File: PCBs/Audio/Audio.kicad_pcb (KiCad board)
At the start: 4 copper layers, 24.5 x 33.4 mm, 23 parts, among them J1 Conn_01x15, J2 Conn_01x02, U1 PTAS2780RYAR

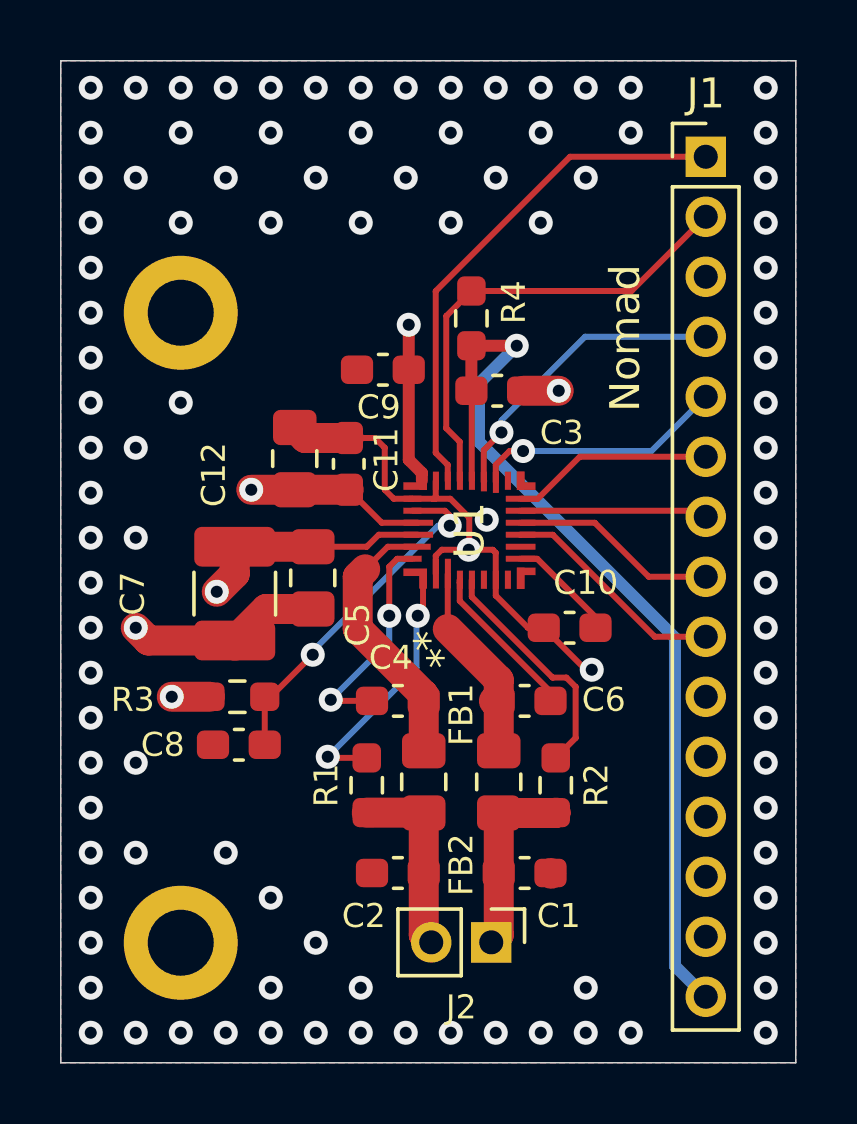
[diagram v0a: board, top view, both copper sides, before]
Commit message: Modification du PCB de la partie audio pour avoir une perle de ferrite avec une ampreinte plus grande
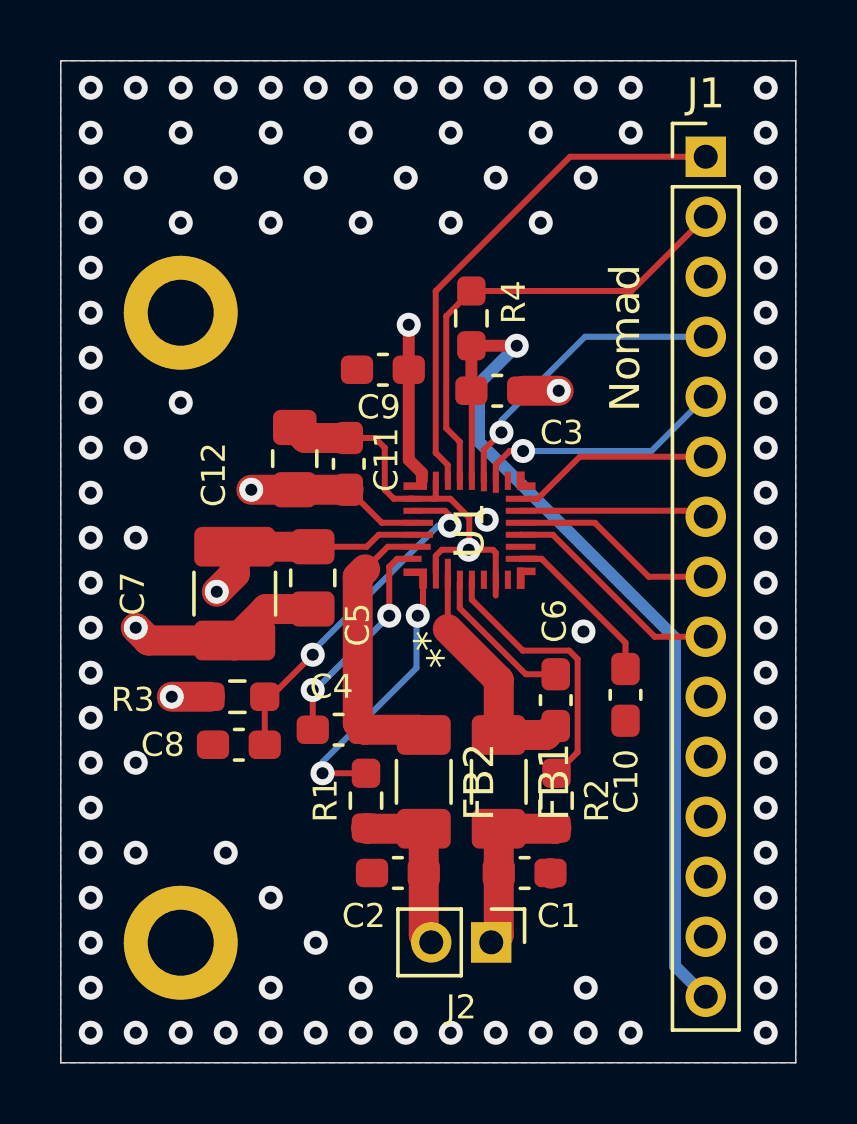
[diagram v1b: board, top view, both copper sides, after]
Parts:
- FB1, FB2: footprint Capacitor_SMD:C_0805_2012Metric_Pad1.18x1.45mm_HandSolder -> Capacitor_SMD:C_1206_3216Metric_Pad1.33x1.80mm_HandSolder
- moved C10 2.91 mm to (151.8, 103.2), turned to -90 degrees
- moved C4 2.20 mm to (142.3, 104.4)
- moved C6 1.04 mm to (149.5, 103.4), turned to 90 degrees
- moved R2 0.51 mm to (149.5, 106.8)
- moved R1 0.51 mm to (143.2, 106.8)
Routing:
- net GND: track 26.4 -> 22.1 mm
- net /DREG: track 3.79 -> 6.09 mm
- net OUTP: track 6.77 -> 8.40 mm
- net /VSNSP: track 7.92 -> 9.11 mm
- net /VSNSN: track 8.53 -> 9.29 mm
- net OUTN: track 9.10 -> 9.63 mm
